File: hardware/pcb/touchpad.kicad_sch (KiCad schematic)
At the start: 6 parts, among them J9 Conn_01x05_Socket, U7 DRV2605LDGS

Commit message: added a bunch testpoints
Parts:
- added TP78: HAPT_EN, TestPoint:TestPoint_Pad_D1.0mm, symbol Connector:TestPoint
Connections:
- net HAPT_EN: now also TP78.1
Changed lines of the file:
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@@
+		(color 0 0 0 0)
+	)
+	(junction
+		(at 50.8 77.47)
+		(diameter 0)
 		(color 0 0 0 0)
 	)
@@
 	(wire
 		(pts
+			(xy 50.8 77.47) (xy 50.8 80.01)
+		)
+		(stroke
+			(width 0)
+			(type default)
+		)
+	)
+	(wire
+		(pts
+			(xy 50.8 77.47) (xy 53.34 77.47)
+		)
+		(stroke
+			(width 0)
+			(type default)
+		)
+	)
+	(wire
+		(pts
 			(xy 80.01 77.47) (xy 80.01 78.74)
 		)
@@
 	(wire
 		(pts
-			(xy 49.53 77.47) (xy 53.34 77.47)
+			(xy 46.99 77.47) (xy 50.8 77.47)
 		)
 		(stroke
@@
 	(hierarchical_label "HAPT_EN"
 		(shape input)
-		(at 49.53 77.47 180)
+		(at 46.99 77.47 180)
 		(effects
 			(font
@@
 					(unit 1)
 				)
+			)
+		)
+	)
+	(symbol
+		(lib_id "Connector:TestPoint")
+		(at 50.8 80.01 0)
+		(mirror x)
+		(unit 1)
+		(body_style 1)
+		(exclude_from_sim no)
+		(in_bom yes)
+		(on_board yes)
+		(in_pos_files yes)
+		(dnp no)
+		(property "Reference" "TP78"
+			(at 50.8 85.852 0)
+			(show_name no)
+			(do_not_autoplace no)
+			(effects
+				(font
+					(size 1.27 1.27)
+				)
+			)
+		)
+		(property "Value" "HAPT_EN"
+			(at 50.8 88.392 0)
+			(show_name no)
+			(do_not_autoplace no)
+			(effects
+				(font
+					(size 1.27 1.27)
+				)
+			)
+		)
+		(property "Footprint" "TestPoint:TestPoint_Pad_D1.0mm"
+			(at 55.88 80.01 0)
+			(hide yes)
+			(show_name no)
+			(do_not_autoplace no)
+			(effects
+				(font
+					(size 1.27 1.27)
+				)
+			)
+		)
+		(property "Datasheet" ""
+			(at 55.88 80.01 0)
+			(hide yes)
+			(show_name no)
+			(do_not_autoplace no)
+			(effects
+				(font
+					(size 1.27 1.27)
+				)
+			)
+		)
+		(property "Description" "test point"
+			(at 50.8 80.01 0)
+			(hide yes)
+			(show_name no)
+			(do_not_autoplace no)
+			(effects
+				(font
+					(size 1.27 1.27)
+				)
+			)
+		)
+		(pin "1"
+		)
+		(instances
+			(project "meko"
+				(path "/da54f10a-146b-4941-a9c7-55c7173bb101/7a0a8608-fb91-40ee-9ae1-ac8166908c37"
+					(reference "TP78")
+					(unit 1)
+				)

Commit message: removed testpoints on sd cards, since I can probe the pins there
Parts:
- added TP65: T_~{INT}, TestPoint:TestPoint_Pad_D1.0mm, symbol Connector:TestPoint
- renumbered TP78 to TP62, TP8 to TP63, TP9 to TP64
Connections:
- net TOUCH_~{INT}: now also TP65.1
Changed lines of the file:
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@@
+	)
+	(junction
+		(at 123.19 71.12)
+		(diameter 0)
+		(color 0 0 0 0)
 	)
 	(junction
@@
 	(wire
 		(pts
+			(xy 123.19 71.12) (xy 132.08 71.12)
+		)
+		(stroke
+			(width 0)
+			(type default)
+		)
+	)
+	(wire
+		(pts
 			(xy 62.23 58.42) (xy 64.77 58.42)
 		)
@@
 	(wire
 		(pts
-			(xy 120.65 71.12) (xy 132.08 71.12)
+			(xy 120.65 71.12) (xy 123.19 71.12)
 		)
 		(stroke
@@
 		(pts
 			(xy 44.45 64.77) (xy 44.45 67.31)
+		)
+		(stroke
+			(width 0)
+			(type default)
+		)
+	)
+	(wire
+		(pts
+			(xy 123.19 64.77) (xy 123.19 71.12)
 		)
 		(stroke
@@
 		(in_pos_files yes)
 		(dnp no)
-		(property "Reference" "#PWR0135"
+		(property "Reference" "#PWR0133"
 			(at 66.04 90.17 0)
 			(hide yes)
@@
 			(project "meko"
 				(path "/da54f10a-146b-4941-a9c7-55c7173bb101/7a0a8608-fb91-40ee-9ae1-ac8166908c37"
-					(reference "#PWR0135")
+					(reference "#PWR0133")
 					(unit 1)
 				)
@@
 		(in_pos_files yes)
 		(dnp no)
-		(property "Reference" "#PWR0132"
+		(property "Reference" "#PWR0135"
 			(at 124.46 78.74 0)
 			(hide yes)
@@
 			(project "meko"
 				(path "/da54f10a-146b-4941-a9c7-55c7173bb101/7a0a8608-fb91-40ee-9ae1-ac8166908c37"
-					(reference "#PWR0132")
+					(reference "#PWR0135")
 					(unit 1)
 				)
@@
 		(in_pos_files yes)
 		(dnp no)
-		(property "Reference" "TP78"
+		(property "Reference" "TP62"
 			(at 50.8 85.852 0)
 			(show_name no)
@@
 			(project "meko"
 				(path "/da54f10a-146b-4941-a9c7-55c7173bb101/7a0a8608-fb91-40ee-9ae1-ac8166908c37"
-					(reference "TP78")
+					(reference "TP62")
 					(unit 1)
 				)
@@
 		(in_pos_files yes)
 		(dnp no)
-		(property "Reference" "#PWR0136"
+		(property "Reference" "#PWR0134"
 			(at 80.01 91.44 0)
 			(hide yes)
@@
 			(project "meko"
 				(path "/da54f10a-146b-4941-a9c7-55c7173bb101/7a0a8608-fb91-40ee-9ae1-ac8166908c37"
-					(reference "#PWR0136")
+					(reference "#PWR0134")
 					(unit 1)
 				)
@@
 		(in_pos_files yes)
 		(dnp no)
-		(property "Reference" "TP9"
+		(property "Reference" "TP64"
 			(at 84.328 69.85 90)
 			(show_name no)
@@
 			(project "meko"
 				(path "/da54f10a-146b-4941-a9c7-55c7173bb101/7a0a8608-fb91-40ee-9ae1-ac8166908c37"
-					(reference "TP9")
+					(reference "TP64")
 					(unit 1)
 				)
@@
 		(in_pos_files yes)
 		(dnp no)
-		(property "Reference" "#PWR0134"
+		(property "Reference" "#PWR0136"
 			(at 134.62 81.28 0)
 			(hide yes)
@@
 			(project "meko"
 				(path "/da54f10a-146b-4941-a9c7-55c7173bb101/7a0a8608-fb91-40ee-9ae1-ac8166908c37"
-					(reference "#PWR0134")
+					(reference "#PWR0136")
 					(unit 1)
 				)
@@
 		(in_pos_files yes)
 		(dnp no)
-		(property "Reference" "#PWR0130"
+		(property "Reference" "#PWR0132"
 			(at 64.77 60.96 0)
 			(hide yes)
@@
 			(project "meko"
 				(path "/da54f10a-146b-4941-a9c7-55c7173bb101/7a0a8608-fb91-40ee-9ae1-ac8166908c37"
-					(reference "#PWR0130")
+					(reference "#PWR0132")
 					(unit 1)
 				)
@@
 		(in_pos_files yes)
 		(dnp no)
-		(property "Reference" "#PWR0133"
+		(property "Reference" "#PWR0130"
 			(at 45.72 74.93 0)
 			(hide yes)
@@
 			(project "meko"
 				(path "/da54f10a-146b-4941-a9c7-55c7173bb101/7a0a8608-fb91-40ee-9ae1-ac8166908c37"
-					(reference "#PWR0133")
+					(reference "#PWR0130")
+					(unit 1)
+				)
+			)
+		)
+	)
+	(symbol
+		(lib_id "Connector:TestPoint")
+		(at 123.19 64.77 0)
+		(mirror y)
+		(unit 1)
+		(body_style 1)
+		(exclude_from_sim no)
+		(in_bom yes)
+		(on_board yes)
+		(in_pos_files yes)
+		(dnp no)
+		(property "Reference" "TP65"
+			(at 123.19 56.642 0)
+			(show_name no)
+			(do_not_autoplace no)
+			(effects
+				(font
+					(size 1.27 1.27)
+				)
+			)
+		)
+		(property "Value" "T_~{INT}"
+			(at 123.19 59.182 0)
+			(show_name no)
+			(do_not_autoplace no)
+			(effects
+				(font
+					(size 1.27 1.27)
+				)
+			)
+		)
+		(property "Footprint" "TestPoint:TestPoint_Pad_D1.0mm"
+			(at 118.11 64.77 0)
+			(hide yes)
+			(show_name no)
+			(do_not_autoplace no)
+			(effects
+				(font
+					(size 1.27 1.27)
+				)
+			)
+		)
+		(property "Datasheet" ""
+			(at 118.11 64.77 0)
+			(hide yes)
+			(show_name no)
+			(do_not_autoplace no)
+			(effects
+				(font
+					(size 1.27 1.27)
+				)
+			)
+		)
+		(property "Description" "test point"
+			(at 123.19 64.77 0)
+			(hide yes)
+			(show_name no)
+			(do_not_autoplace no)
+			(effects
+				(font
+					(size 1.27 1.27)
+				)
+			)
+		)
+		(pin "1"
+		)
+		(instances
+			(project "meko"
+				(path "/da54f10a-146b-4941-a9c7-55c7173bb101/7a0a8608-fb91-40ee-9ae1-ac8166908c37"
+					(reference "TP65")
 					(unit 1)
 				)
@@
 		(in_pos_files yes)
 		(dnp no)
-		(property "Reference" "TP8"
+		(property "Reference" "TP63"
 			(at 84.328 65.278 90)
 			(show_name no)
@@
 			(project "meko"
 				(path "/da54f10a-146b-4941-a9c7-55c7173bb101/7a0a8608-fb91-40ee-9ae1-ac8166908c37"
-					(reference "TP8")
+					(reference "TP63")
 					(unit 1)
 				)

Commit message: added capacitor to sama ddr vref pin
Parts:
- renumbered C121 to C123, C122 to C124
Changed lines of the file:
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@@
 		(in_pos_files yes)
 		(dnp no)
-		(property "Reference" "#PWR0133"
+		(property "Reference" "#PWR0135"
 			(at 66.04 90.17 0)
 			(hide yes)
@@
 			(project "meko"
 				(path "/da54f10a-146b-4941-a9c7-55c7173bb101/7a0a8608-fb91-40ee-9ae1-ac8166908c37"
-					(reference "#PWR0133")
+					(reference "#PWR0135")
 					(unit 1)
 				)
@@
 		(in_pos_files yes)
 		(dnp no)
-		(property "Reference" "#PWR0135"
+		(property "Reference" "#PWR0137"
 			(at 124.46 78.74 0)
 			(hide yes)
@@
 			(project "meko"
 				(path "/da54f10a-146b-4941-a9c7-55c7173bb101/7a0a8608-fb91-40ee-9ae1-ac8166908c37"
-					(reference "#PWR0135")
+					(reference "#PWR0137")
 					(unit 1)
 				)
@@
 		(in_pos_files yes)
 		(dnp no)
-		(property "Reference" "C121"
+		(property "Reference" "C123"
 			(at 58.674 57.404 90)
 			(show_name no)
@@
 			(project "meko"
 				(path "/da54f10a-146b-4941-a9c7-55c7173bb101/7a0a8608-fb91-40ee-9ae1-ac8166908c37"
-					(reference "C121")
+					(reference "C123")
 					(unit 1)
 				)
@@
 		(in_pos_files yes)
 		(dnp no)
-		(property "Reference" "C122"
+		(property "Reference" "C124"
 			(at 81.788 80.264 0)
 			(show_name no)
@@
 			(project "meko"
 				(path "/da54f10a-146b-4941-a9c7-55c7173bb101/7a0a8608-fb91-40ee-9ae1-ac8166908c37"
-					(reference "C122")
+					(reference "C124")
 					(unit 1)
 				)
@@
 		(in_pos_files yes)
 		(dnp no)
-		(property "Reference" "#PWR0134"
+		(property "Reference" "#PWR0136"
 			(at 80.01 91.44 0)
 			(hide yes)
@@
 			(project "meko"
 				(path "/da54f10a-146b-4941-a9c7-55c7173bb101/7a0a8608-fb91-40ee-9ae1-ac8166908c37"
-					(reference "#PWR0134")
+					(reference "#PWR0136")
 					(unit 1)
 				)
@@
 		(in_pos_files yes)
 		(dnp no)
-		(property "Reference" "#PWR0136"
+		(property "Reference" "#PWR0138"
 			(at 134.62 81.28 0)
 			(hide yes)
@@
 			(project "meko"
 				(path "/da54f10a-146b-4941-a9c7-55c7173bb101/7a0a8608-fb91-40ee-9ae1-ac8166908c37"
-					(reference "#PWR0136")
+					(reference "#PWR0138")
 					(unit 1)
 				)
@@
 		(in_pos_files yes)
 		(dnp no)
-		(property "Reference" "#PWR0131"
+		(property "Reference" "#PWR0133"
 			(at 54.61 66.04 0)
 			(hide yes)
@@
 			(project "meko"
 				(path "/da54f10a-146b-4941-a9c7-55c7173bb101/7a0a8608-fb91-40ee-9ae1-ac8166908c37"
-					(reference "#PWR0131")
+					(reference "#PWR0133")
 					(unit 1)
 				)
@@
 		(in_pos_files yes)
 		(dnp no)
-		(property "Reference" "#PWR0132"
+		(property "Reference" "#PWR0134"
 			(at 64.77 60.96 0)
 			(hide yes)
@@
 			(project "meko"
 				(path "/da54f10a-146b-4941-a9c7-55c7173bb101/7a0a8608-fb91-40ee-9ae1-ac8166908c37"
-					(reference "#PWR0132")
+					(reference "#PWR0134")
 					(unit 1)
 				)
@@
 		(in_pos_files yes)
 		(dnp no)
-		(property "Reference" "#PWR0130"
+		(property "Reference" "#PWR0132"
 			(at 45.72 74.93 0)
 			(hide yes)
@@
 			(project "meko"
 				(path "/da54f10a-146b-4941-a9c7-55c7173bb101/7a0a8608-fb91-40ee-9ae1-ac8166908c37"
-					(reference "#PWR0130")
-					(unit 1)
-				)
+					(reference "#PWR0132")
+					(unit 1)
+				)

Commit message: didn't save last time :sob:
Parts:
- renumbered C123 to C124, C124 to C125
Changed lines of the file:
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@@
 		(in_pos_files yes)
 		(dnp no)
-		(property "Reference" "#PWR0135"
+		(property "Reference" "#PWR0136"
 			(at 66.04 90.17 0)
 			(hide yes)
@@
 			(project "meko"
 				(path "/da54f10a-146b-4941-a9c7-55c7173bb101/7a0a8608-fb91-40ee-9ae1-ac8166908c37"
-					(reference "#PWR0135")
+					(reference "#PWR0136")
 					(unit 1)
 				)
@@
 		(in_pos_files yes)
 		(dnp no)
-		(property "Reference" "#PWR0137"
+		(property "Reference" "#PWR0138"
 			(at 124.46 78.74 0)
 			(hide yes)
@@
 			(project "meko"
 				(path "/da54f10a-146b-4941-a9c7-55c7173bb101/7a0a8608-fb91-40ee-9ae1-ac8166908c37"
-					(reference "#PWR0137")
+					(reference "#PWR0138")
 					(unit 1)
 				)
@@
 		(in_pos_files yes)
 		(dnp no)
-		(property "Reference" "C123"
+		(property "Reference" "C124"
 			(at 58.674 57.404 90)
 			(show_name no)
@@
 			(project "meko"
 				(path "/da54f10a-146b-4941-a9c7-55c7173bb101/7a0a8608-fb91-40ee-9ae1-ac8166908c37"
-					(reference "C123")
+					(reference "C124")
 					(unit 1)
 				)
@@
 		(in_pos_files yes)
 		(dnp no)
-		(property "Reference" "C124"
+		(property "Reference" "C125"
 			(at 81.788 80.264 0)
 			(show_name no)
@@
 			(project "meko"
 				(path "/da54f10a-146b-4941-a9c7-55c7173bb101/7a0a8608-fb91-40ee-9ae1-ac8166908c37"
-					(reference "C124")
+					(reference "C125")
 					(unit 1)
 				)
@@
 		(in_pos_files yes)
 		(dnp no)
-		(property "Reference" "#PWR0136"
+		(property "Reference" "#PWR0137"
 			(at 80.01 91.44 0)
 			(hide yes)
@@
 			(project "meko"
 				(path "/da54f10a-146b-4941-a9c7-55c7173bb101/7a0a8608-fb91-40ee-9ae1-ac8166908c37"
-					(reference "#PWR0136")
+					(reference "#PWR0137")
 					(unit 1)
 				)
@@
 		(in_pos_files yes)
 		(dnp no)
-		(property "Reference" "#PWR0138"
+		(property "Reference" "#PWR0139"
 			(at 134.62 81.28 0)
 			(hide yes)
@@
 			(project "meko"
 				(path "/da54f10a-146b-4941-a9c7-55c7173bb101/7a0a8608-fb91-40ee-9ae1-ac8166908c37"
-					(reference "#PWR0138")
+					(reference "#PWR0139")
 					(unit 1)
 				)
@@
 		(in_pos_files yes)
 		(dnp no)
-		(property "Reference" "#PWR0133"
+		(property "Reference" "#PWR0134"
 			(at 54.61 66.04 0)
 			(hide yes)
@@
 			(project "meko"
 				(path "/da54f10a-146b-4941-a9c7-55c7173bb101/7a0a8608-fb91-40ee-9ae1-ac8166908c37"
-					(reference "#PWR0133")
+					(reference "#PWR0134")
 					(unit 1)
 				)
@@
 		(in_pos_files yes)
 		(dnp no)
-		(property "Reference" "#PWR0134"
+		(property "Reference" "#PWR0135"
 			(at 64.77 60.96 0)
 			(hide yes)
@@
 			(project "meko"
 				(path "/da54f10a-146b-4941-a9c7-55c7173bb101/7a0a8608-fb91-40ee-9ae1-ac8166908c37"
-					(reference "#PWR0134")
+					(reference "#PWR0135")
 					(unit 1)
 				)
@@
 		(in_pos_files yes)
 		(dnp no)
-		(property "Reference" "#PWR0132"
+		(property "Reference" "#PWR0133"
 			(at 45.72 74.93 0)
 			(hide yes)
@@
 			(project "meko"
 				(path "/da54f10a-146b-4941-a9c7-55c7173bb101/7a0a8608-fb91-40ee-9ae1-ac8166908c37"
-					(reference "#PWR0132")
-					(unit 1)
-				)
+					(reference "#PWR0133")
+					(unit 1)
+				)

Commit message: added pullups for jtag
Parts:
- renumbered TP65 to TP62, TP62 to TP65
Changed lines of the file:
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@@
 		(in_pos_files yes)
 		(dnp no)
-		(property "Reference" "#PWR0136"
+		(property "Reference" "#PWR0139"
 			(at 66.04 90.17 0)
 			(hide yes)
@@
 			(project "meko"
 				(path "/da54f10a-146b-4941-a9c7-55c7173bb101/7a0a8608-fb91-40ee-9ae1-ac8166908c37"
-					(reference "#PWR0136")
+					(reference "#PWR0139")
 					(unit 1)
 				)
@@
 		(in_pos_files yes)
 		(dnp no)
-		(property "Reference" "#PWR0138"
+		(property "Reference" "#PWR0137"
 			(at 124.46 78.74 0)
 			(hide yes)
@@
 			(project "meko"
 				(path "/da54f10a-146b-4941-a9c7-55c7173bb101/7a0a8608-fb91-40ee-9ae1-ac8166908c37"
-					(reference "#PWR0138")
+					(reference "#PWR0137")
 					(unit 1)
 				)
@@
 		(in_pos_files yes)
 		(dnp no)
-		(property "Reference" "TP62"
+		(property "Reference" "TP65"
 			(at 50.8 85.852 0)
 			(show_name no)
@@
 			(project "meko"
 				(path "/da54f10a-146b-4941-a9c7-55c7173bb101/7a0a8608-fb91-40ee-9ae1-ac8166908c37"
-					(reference "TP62")
+					(reference "TP65")
 					(unit 1)
 				)
@@
 		(in_pos_files yes)
 		(dnp no)
-		(property "Reference" "#PWR0137"
+		(property "Reference" "#PWR0140"
 			(at 80.01 91.44 0)
 			(hide yes)
@@
 			(project "meko"
 				(path "/da54f10a-146b-4941-a9c7-55c7173bb101/7a0a8608-fb91-40ee-9ae1-ac8166908c37"
-					(reference "#PWR0137")
+					(reference "#PWR0140")
 					(unit 1)
 				)
@@
 		(in_pos_files yes)
 		(dnp no)
-		(property "Reference" "#PWR0139"
+		(property "Reference" "#PWR0138"
 			(at 134.62 81.28 0)
 			(hide yes)
@@
 			(project "meko"
 				(path "/da54f10a-146b-4941-a9c7-55c7173bb101/7a0a8608-fb91-40ee-9ae1-ac8166908c37"
-					(reference "#PWR0139")
+					(reference "#PWR0138")
 					(unit 1)
 				)
@@
 		(in_pos_files yes)
 		(dnp no)
-		(property "Reference" "#PWR0134"
+		(property "Reference" "#PWR0135"
 			(at 54.61 66.04 0)
 			(hide yes)
@@
 			(project "meko"
 				(path "/da54f10a-146b-4941-a9c7-55c7173bb101/7a0a8608-fb91-40ee-9ae1-ac8166908c37"
-					(reference "#PWR0134")
+					(reference "#PWR0135")
 					(unit 1)
 				)
@@
 		(in_pos_files yes)
 		(dnp no)
-		(property "Reference" "#PWR0135"
+		(property "Reference" "#PWR0134"
 			(at 64.77 60.96 0)
 			(hide yes)
@@
 			(project "meko"
 				(path "/da54f10a-146b-4941-a9c7-55c7173bb101/7a0a8608-fb91-40ee-9ae1-ac8166908c37"
-					(reference "#PWR0135")
+					(reference "#PWR0134")
 					(unit 1)
 				)
@@
 		(in_pos_files yes)
 		(dnp no)
-		(property "Reference" "#PWR0133"
+		(property "Reference" "#PWR0136"
 			(at 45.72 74.93 0)
 			(hide yes)
@@
 			(project "meko"
 				(path "/da54f10a-146b-4941-a9c7-55c7173bb101/7a0a8608-fb91-40ee-9ae1-ac8166908c37"
-					(reference "#PWR0133")
+					(reference "#PWR0136")
 					(unit 1)
 				)
@@
 		(in_pos_files yes)
 		(dnp no)
-		(property "Reference" "TP65"
+		(property "Reference" "TP62"
 			(at 123.19 56.642 0)
 			(show_name no)
@@
 			(project "meko"
 				(path "/da54f10a-146b-4941-a9c7-55c7173bb101/7a0a8608-fb91-40ee-9ae1-ac8166908c37"
-					(reference "TP65")
-					(unit 1)
-				)
+					(reference "TP62")
+					(unit 1)
+				)

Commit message: added touchpad conn
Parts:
- removed J9: Conn_01x05_Socket, symbol Connector:Conn_01x05_Socket
- added J9: 503480-0540, 5034800540:503480-0540, symbol 503480-0540:503480-0540
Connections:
- net +3V3: now also J9.2
- net GND: now also J9.11 (MP_1), J9.12 (MP_2), J9.4
- net TOUCH.SCL: now also J9.5
- net TOUCH.SDA: now also J9.3
- net TOUCH_~{INT}: now also J9.1
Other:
- note removed: "Actual connector for the trackpad depends on the layout of the PCB Will be chosen later"
- moved on the sheet: TP62

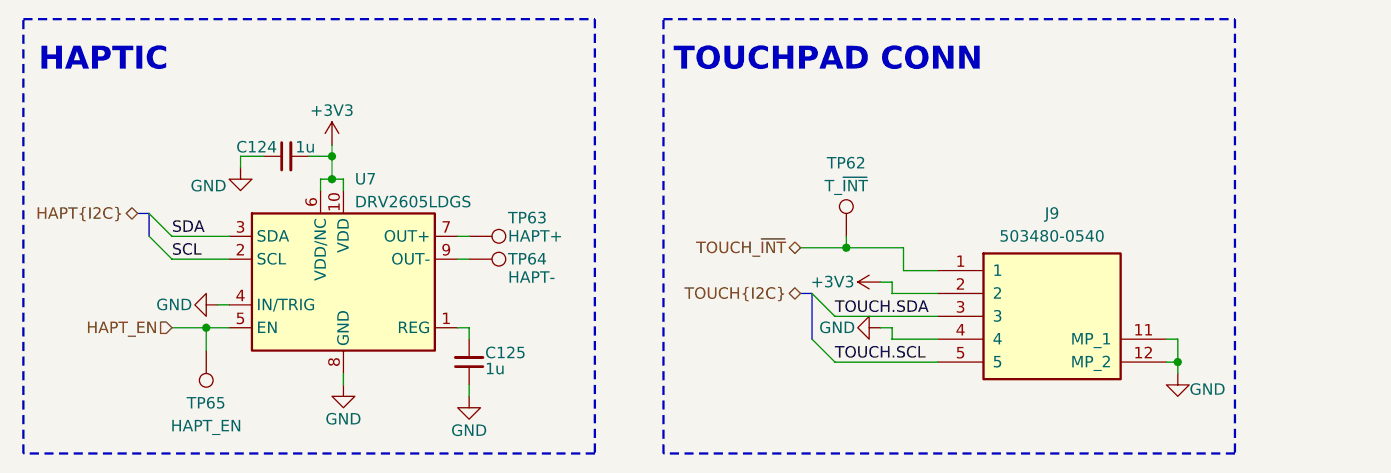
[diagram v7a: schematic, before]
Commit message: added conn to trackpad pcb, updated mockup, placed conn
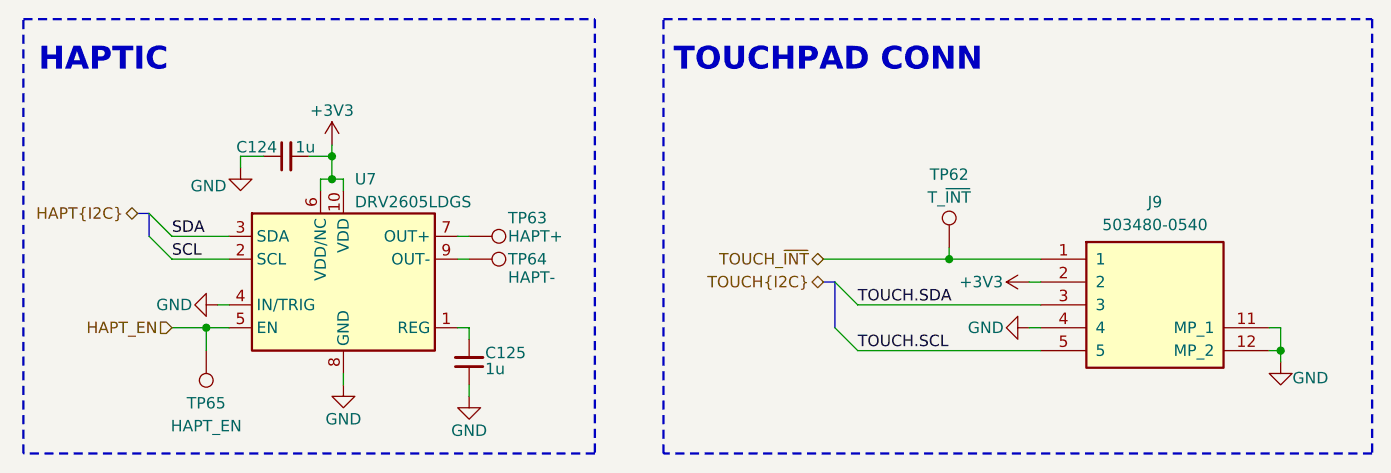
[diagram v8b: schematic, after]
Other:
- moved on the sheet: J9, TP62
